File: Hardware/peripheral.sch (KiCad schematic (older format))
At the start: 54 parts, among them IC1 PCF8563T_5,518, J1 UFL, Q1 MMBT4403, U1 TPL5010DDCR, U2 HX711, U4 MB85RC04VPNF-G-JNERE1, U5 RFM95W-868S2, U6 W25Q32JVSS, U7 24LC02BT-I/SN, Y1 Crystal_Small

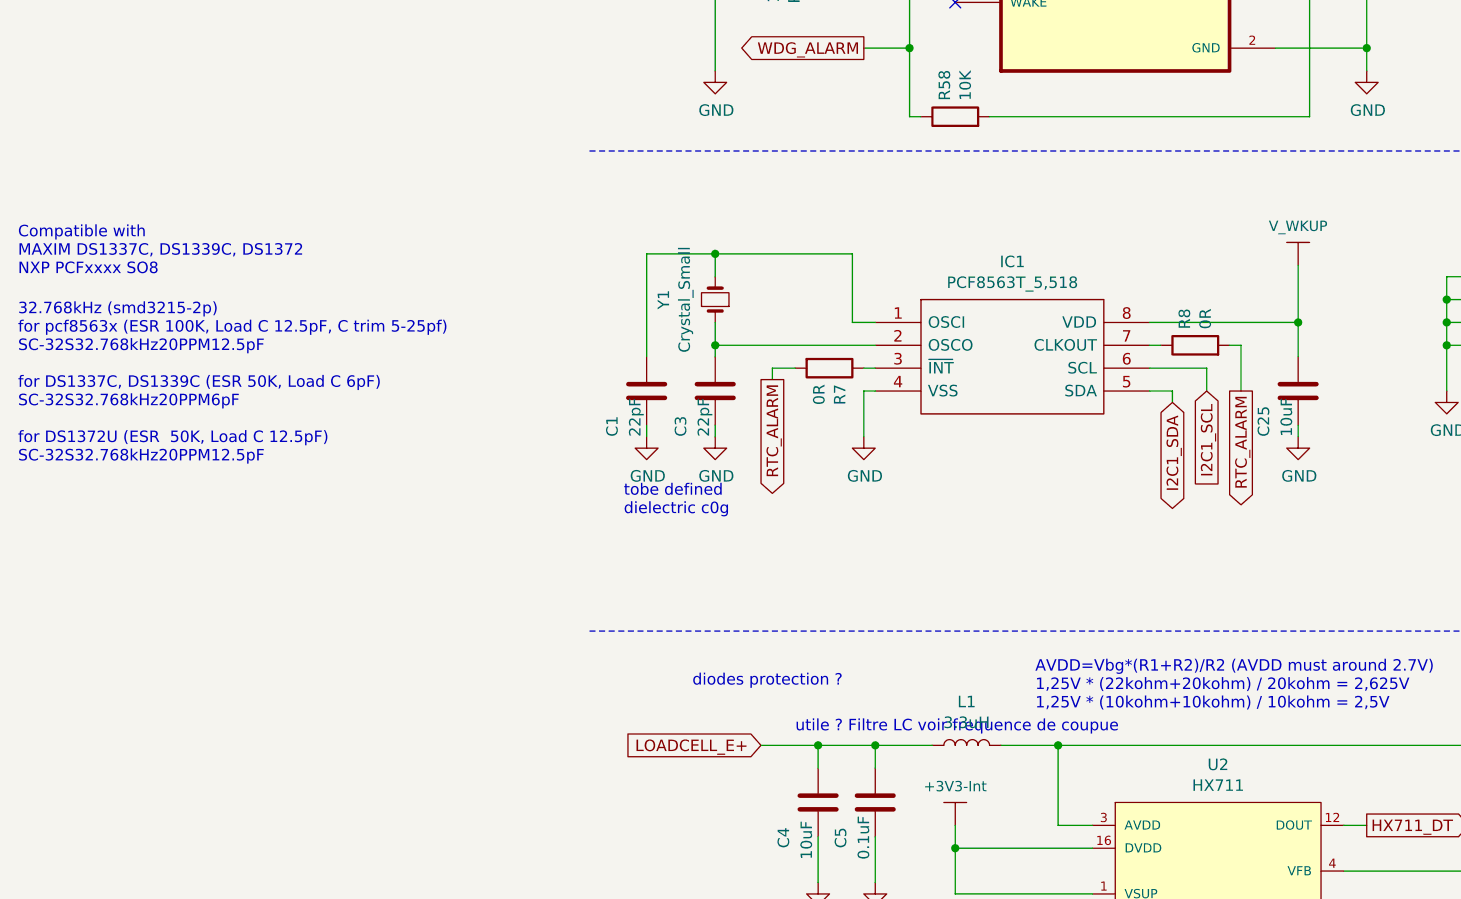
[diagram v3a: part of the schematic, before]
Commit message: Add Gerber files, Bom, Jlcpcb LCSC parts ref, some optimizations
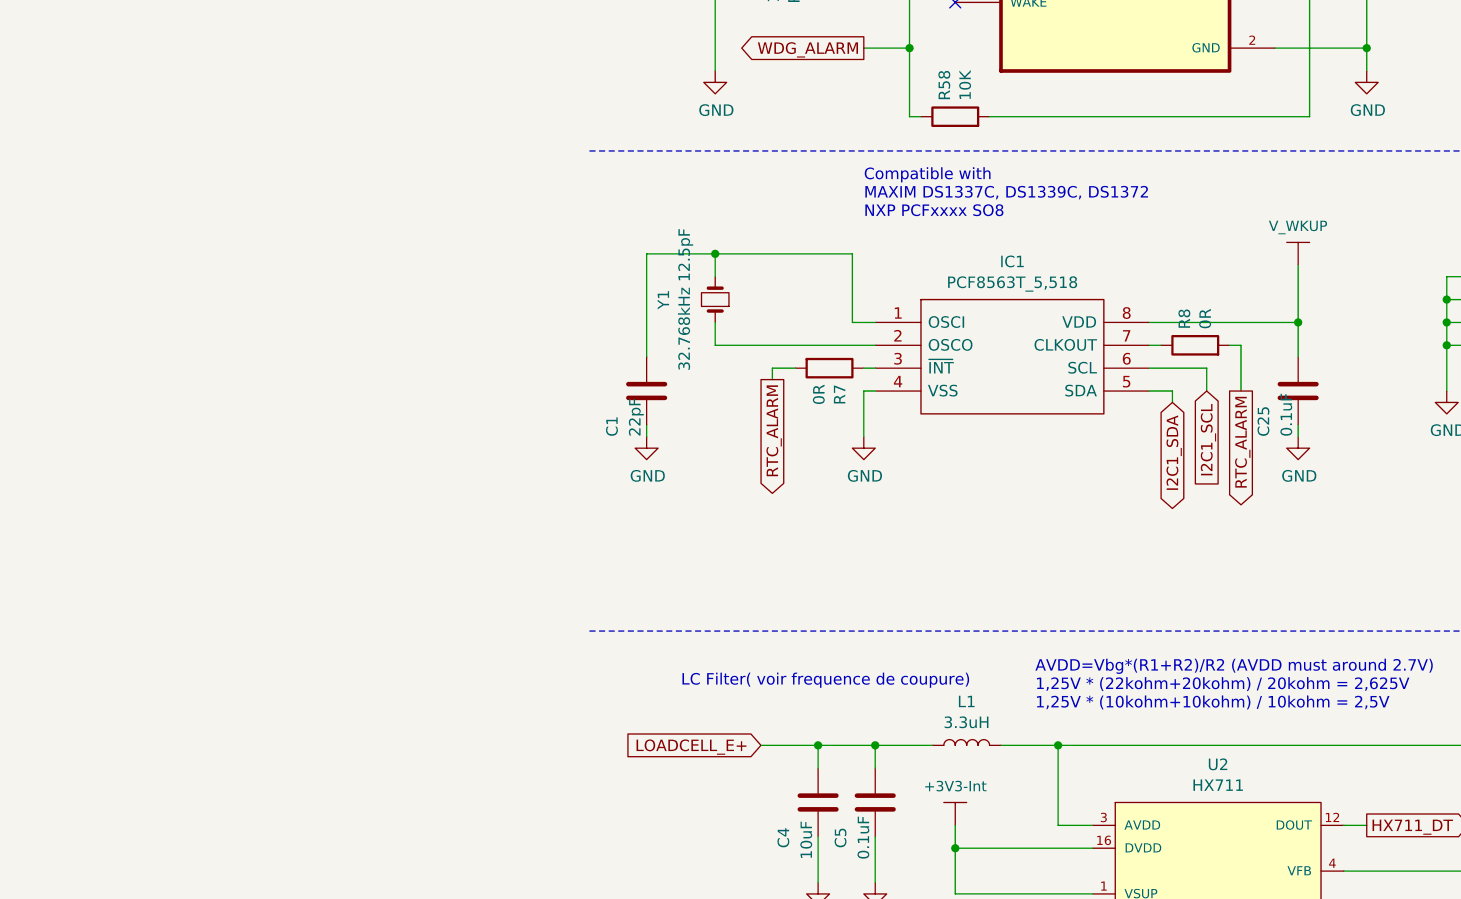
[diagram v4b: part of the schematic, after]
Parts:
- removed C3: 22pF, Capacitor_SMD:C_0201_0603Metric, symbol Device:C
- C1: footprint Capacitor_SMD:C_0201_0603Metric -> Capacitor_SMD:C_0402_1005Metric; Dielectric (none) -> C0G; JLC (none) -> 0402; LCSC (none) -> C76960; Manufacturer_Name (none) -> Murata Electronics; Manufacturer_Part_Number (none) -> GRM1555C1H220JA01D; Size Inch 0201 -> 0402; Size Metric 0603 -> 1005; Tolerance (none) -> 5%; Voltage (none) -> 50V
- C10: Dielectric (none) -> X7R; JLC (none) -> 0603; LCSC (none) -> C1591; Manufacturer_Name (none) -> Samsung Electro-Mechanics; Manufacturer_Part_Number (none) -> CL10B104KB8NNNC; Tolerance (none) -> 10%; Voltage 6.3V -> 50V
- C11, C13, C14, C15, C2, C5, C6, C7, C8: Dielectric (none) -> X7R; JLC (none) -> 0603; LCSC (none) -> C1591; Manufacturer_Name (none) -> Samsung Electro-Mechanics; Manufacturer_Part_Number (none) -> CL10B104KB8NNNC; Tolerance (none) -> 10%; Voltage (none) -> 50V
- C12, C9: Dielectric (none) -> X5R; JLC (none) -> 0603; LCSC (none) -> C19702; Manufacturer_Name (none) -> Samsung Electro-Mechanics; Manufacturer_Part_Number (none) -> CL10A106KP8NNNC; Tolerance (none) -> 10%; Voltage (none) -> 10V
- C25: value 10uF -> 0.1uF; Dielectric (none) -> X7R; JLC (none) -> 0603; LCSC (none) -> C1591; Manufacturer_Name (none) -> Samsung Electro-Mechanics; Manufacturer_Part_Number (none) -> CL10B104KB8NNNC; Tolerance (none) -> 10%; Voltage (none) -> 50V
- C4: Dielectric (none) -> X5R; JLC (none) -> 0603; LCSC (none) -> C19702; Manufacturer_Name (none) -> Samsung Electro-Mechanics; Manufacturer_Part_Number (none) -> CL10A106KP8NNNC; Tolerance (none) -> 10%; Voltage 6.3V -> 10V
- IC1: JLC (none) -> SOIC-8; LCSC (none) -> C7440
- L1: JLC (none) -> 0603; LCSC (none) -> C21189; Manufacturer_Name (none) -> UNI-ROYAL(Uniroyal Elec); Manufacturer_Part_Number (none) -> 0603WAF0000T5E; Populate yes -> no
- Q1: JLC (none) -> SOT-23-3; LCSC (none) -> C85183; Manufacturer_Name (none) -> Diodes Incorporated; Manufacturer_Part_Number MMBT4403 -> MMBT4403-7-F
- R1, R17, R18, R19, R20, R24, R27, R30, R31, R33, R7, R8: JLC (none) -> 0603; LCSC (none) -> C21189; Manufacturer_Name (none) -> UNI-ROYAL(Uniroyal Elec); Manufacturer_Part_Number (none) -> 0603WAF0000T5E; Power Rating (none) -> 1/10W; Voltage (none) -> 75V
- R16, R58: JLC (none) -> 0603; LCSC (none) -> C25804; Manufacturer_Name (none) -> UNI-ROYAL(Uniroyal Elec); Manufacturer_Part_Number (none) -> 0603WAF1002T5E; Power Rating (none) -> 1/10W; Voltage (none) -> 75V
- R2, R6: JLC (none) -> 0603; LCSC (none) -> C22894; Manufacturer_Name (none) -> UNI-ROYAL(Uniroyal Elec); Manufacturer_Part_Number (none) -> 0603WAF1823T5E; Power Rating (none) -> 1/10W; Voltage (none) -> 75V
- R21: JLC (none) -> 0603; LCSC (none) -> C31850; Manufacturer_Name (none) -> UNI-ROYAL(Uniroyal Elec); Manufacturer_Part_Number (none) -> 0603WAF2202T5E; Power Rating (none) -> 1/10W; Voltage (none) -> 75V
- R22: JLC (none) -> 0603; LCSC (none) -> C4184; Manufacturer_Name (none) -> UNI-ROYAL(Uniroyal Elec); Manufacturer_Part_Number (none) -> 0603WAF2002T5E; Power Rating (none) -> 1/10W; Voltage (none) -> 75V
- R26, R28, R29, R32: JLC (none) -> 0603; LCSC (none) -> C23162; Manufacturer_Name (none) -> UNI-ROYAL(Uniroyal Elec); Manufacturer_Part_Number (none) -> 0603WAF4701T5E; Power Rating (none) -> 1/10W; Voltage (none) -> 75V
- R3: JLC (none) -> 0603; LCSC (none) -> C22896; Manufacturer_Name (none) -> UNI-ROYAL(Uniroyal Elec); Manufacturer_Part_Number (none) -> 0603WAF1873T5E; Power Rating (none) -> 1/10W; Voltage (none) -> 75V
- R4, R5: JLC (none) -> 0603; LCSC (none) -> C54021; Manufacturer_Name (none) -> UNI-ROYAL(Uniroyal Elec); Manufacturer_Part_Number (none) -> TC0325B1000T5E; Power Rating (none) -> 1/16W; Tolerance 1% -> 0.1%; Voltage (none) -> 75V
- R9: JLC (none) -> 0603; LCSC (none) -> C22972; Manufacturer_Name (none) -> UNI-ROYAL(Uniroyal Elec); Manufacturer_Part_Number (none) -> 0603WAF2873T5E; Power Rating (none) -> 1/10W; Voltage (none) -> 75V
- U1: JLC (none) -> SOT-23-6; LCSC (none) -> C473912
- U2: JLC (none) -> SOP-16; LCSC (none) -> C43656; Manufacturer_Name (none) -> Avia Semicon (Xiamen); Manufacturer_Part_Number (none) -> HX711Copy
- U4: JLC (none) -> SOIC-8; LCSC (none) -> C8738
- U6: JLC (none) -> SOP-8; LCSC (none) -> C82344
- U7: JLC (none) -> SOIC-8; LCSC (none) -> C5453
- Y1: value Crystal_Small -> 32.768kHz 12.5pF; JLC (none) -> 3215; LCSC (none) -> C97606; Manufacturer_Name (none) -> Seiko; Manufacturer_Part_Number (none) -> SC-32S32.768kHz20PPM12.5pF; package (none) -> 3215_2P
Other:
- note added: "LC Filter( voir frequence de coupure)"
- note removed: "32.768kHz (smd3215-2p)\nfor pcf8563x (ESR 100K, Load C 12.5pF, C trim 5-25pf)\nSC-32S32.768kHz20PPM12.5pF\n\nfor DS1337C, DS1339C (ESR 50K, Load C 6pF)\nSC-32S32.768kHz20PPM6pF\n\nfor DS1372U (ESR 50K, Load C 12.5pF)\nSC-32S32.768kHz20PPM12.5pF\n\n"
- note removed: "tobe defined \ndielectric c0g"
- note removed: "utile ? Filtre LC voir frequence de coupue"

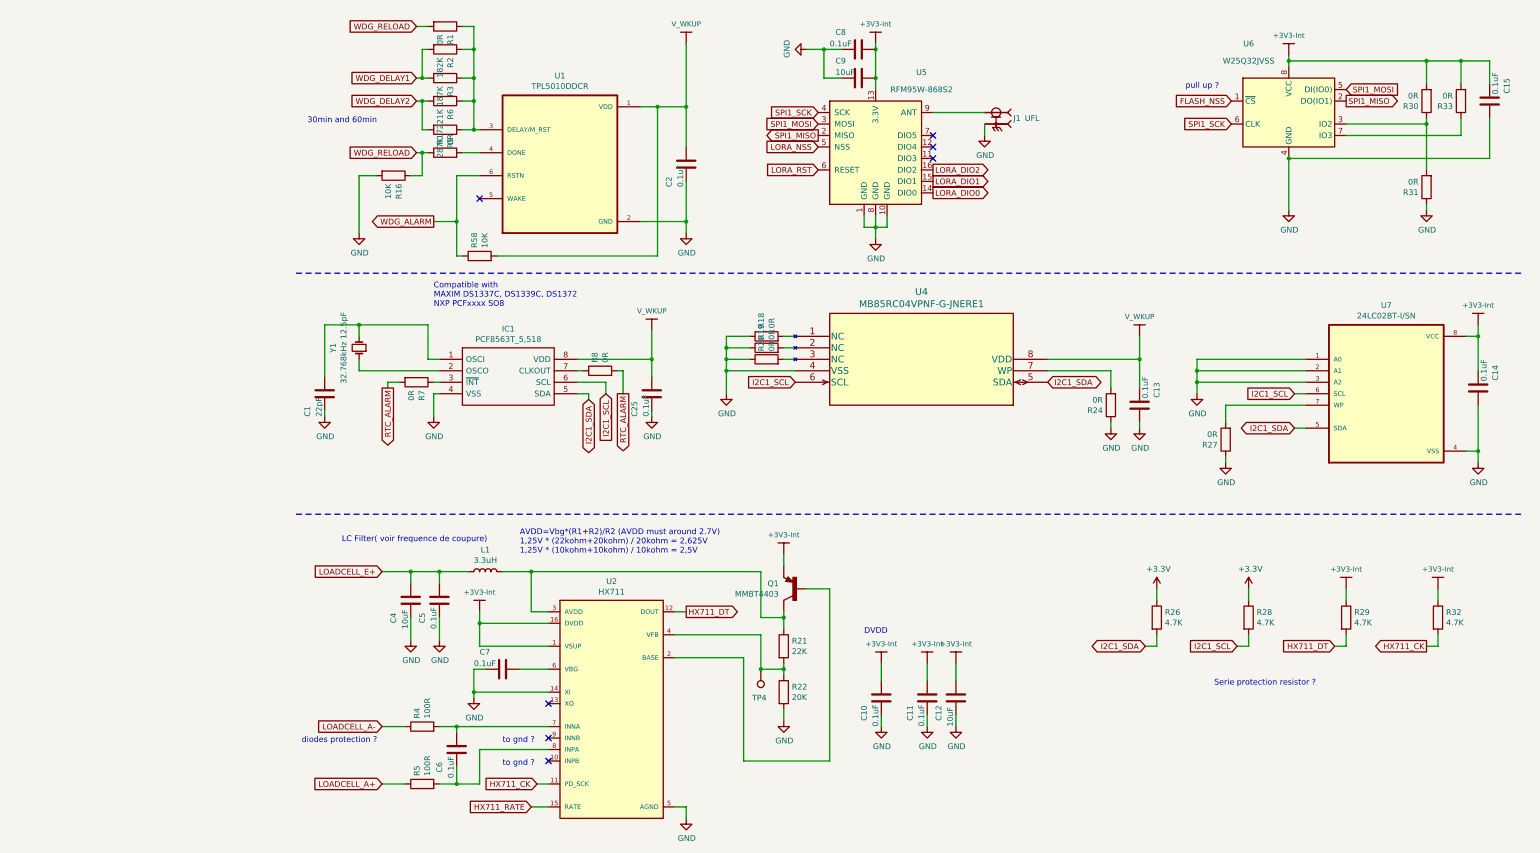
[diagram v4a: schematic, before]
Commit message: Fix JLCPCB assembly issues, Add reverse battery protection, Define Correct crystal capa, Add Layer number and fiducial, and some quicq fix
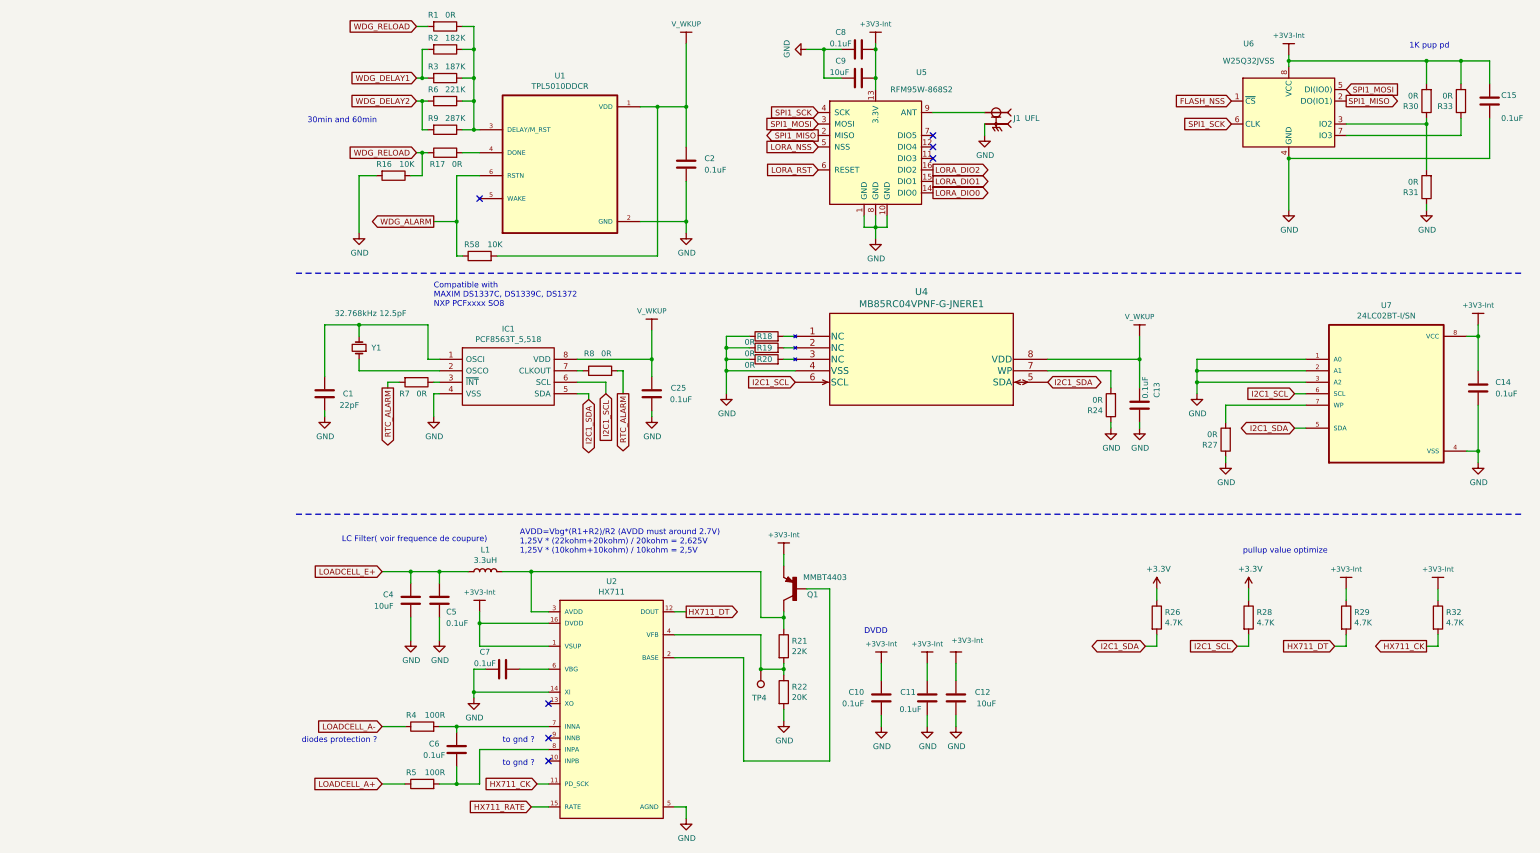
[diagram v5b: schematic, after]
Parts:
- R18, R19, R20, R8: LCSC C21189 -> NM_C21189
- R30, R33: Populate (none) -> yes
- R31: LCSC C21189 -> NM_C21189; Populate (none) -> no
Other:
- note added: "1K pup pd"
- note added: "pullup value optimize"
- note removed: "Serie protection resistor ?"
- note removed: "pull up ?"

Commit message: Debug some features on hardware
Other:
- note added: "2k pup new value pour 400kHz"
- note added: "Change MB24Cxx or NV24Cxx"
- note added: "Change with BR24Hxx or BR24Gxx"
- note added: "Not mounted !!! a terme"
- note added: "Prevoir Masse analog"
- note added: "Prevoir adresse sur A0 / A1 / A1"
- note added: "Prevoir coupure vcc sur avec strap et possiblite sur 3.3 pilotable pour fram et eeprom"
- note added: "Remplacer footprint pour adress i2C"
- note added: "TCA9416\nPI6ULS5V9306\nTCA9406\nPCA9306\nUM3212M8\nCheck voltage translator for external / internal / vkup_vbatt"
- note added: "enlever pose pb et libere pin"
- note added: "prevoir level sifter sur scl et sda car pas sur 3.3"
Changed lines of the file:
@@
 Text Notes 10200 850  0    50   ~ 0
 1K pup pd
+Text Notes 5200 4250 0    50   ~ 0
+Remplacer footprint pour adress i2C
+Text Notes 9150 4650 0    50   ~ 0
+Prevoir adresse sur A0 / A1 / A1
+Text Notes 6650 4800 0    50   ~ 0
+Prevoir coupure vcc sur avec strap et possiblite sur 3.3 pilotable pour fram et eeprom
+Text Notes 1300 4600 0    50   ~ 0
+prevoir level sifter sur scl et sda car pas sur 3.3
+Text Notes 2300 950  0    50   ~ 0
+enlever pose pb et libere pin
+Text Notes 7600 6250 0    50   ~ 0
+2k pup new value pour 400kHz
+Text Notes 9700 2900 0    50   ~ 0
+Change MB24Cxx or NV24Cxx
+Text Notes 9700 3000 0    50   ~ 0
+Change with BR24Hxx or BR24Gxx
+Text Notes 7150 3150 0    50   ~ 0
+TCA9416\nPI6ULS5V9306\nTCA9406\nPCA9306\nUM3212M8\nCheck voltage translator for external / internal / vkup_vbatt
+Text Notes 9550 6200 0    50   ~ 0
+Not mounted !!! a terme
+Text Notes 4000 7550 0    50   ~ 0
+Prevoir Masse analog
 $EndSCHEMATC
